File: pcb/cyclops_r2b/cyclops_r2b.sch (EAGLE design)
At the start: 54 parts, among them IC1 LM324N, IC2 317, IC3 REF02

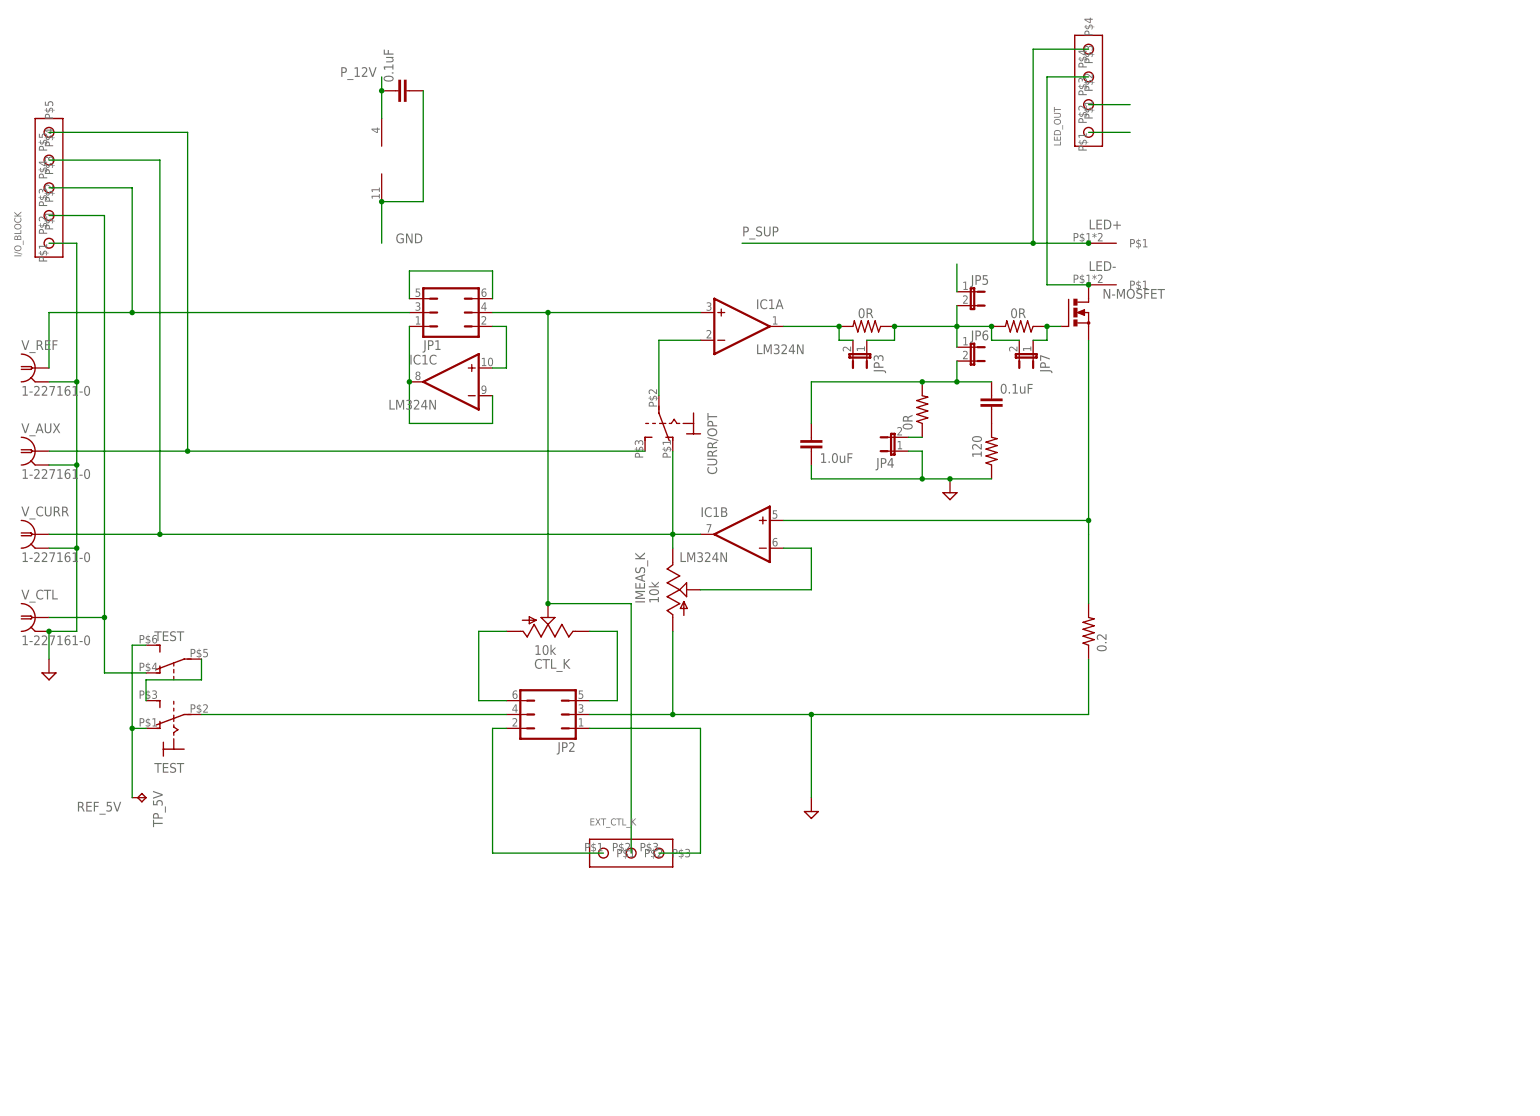
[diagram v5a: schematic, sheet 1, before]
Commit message: Revision 2b of the cyclops driver, ready for OSH Park.
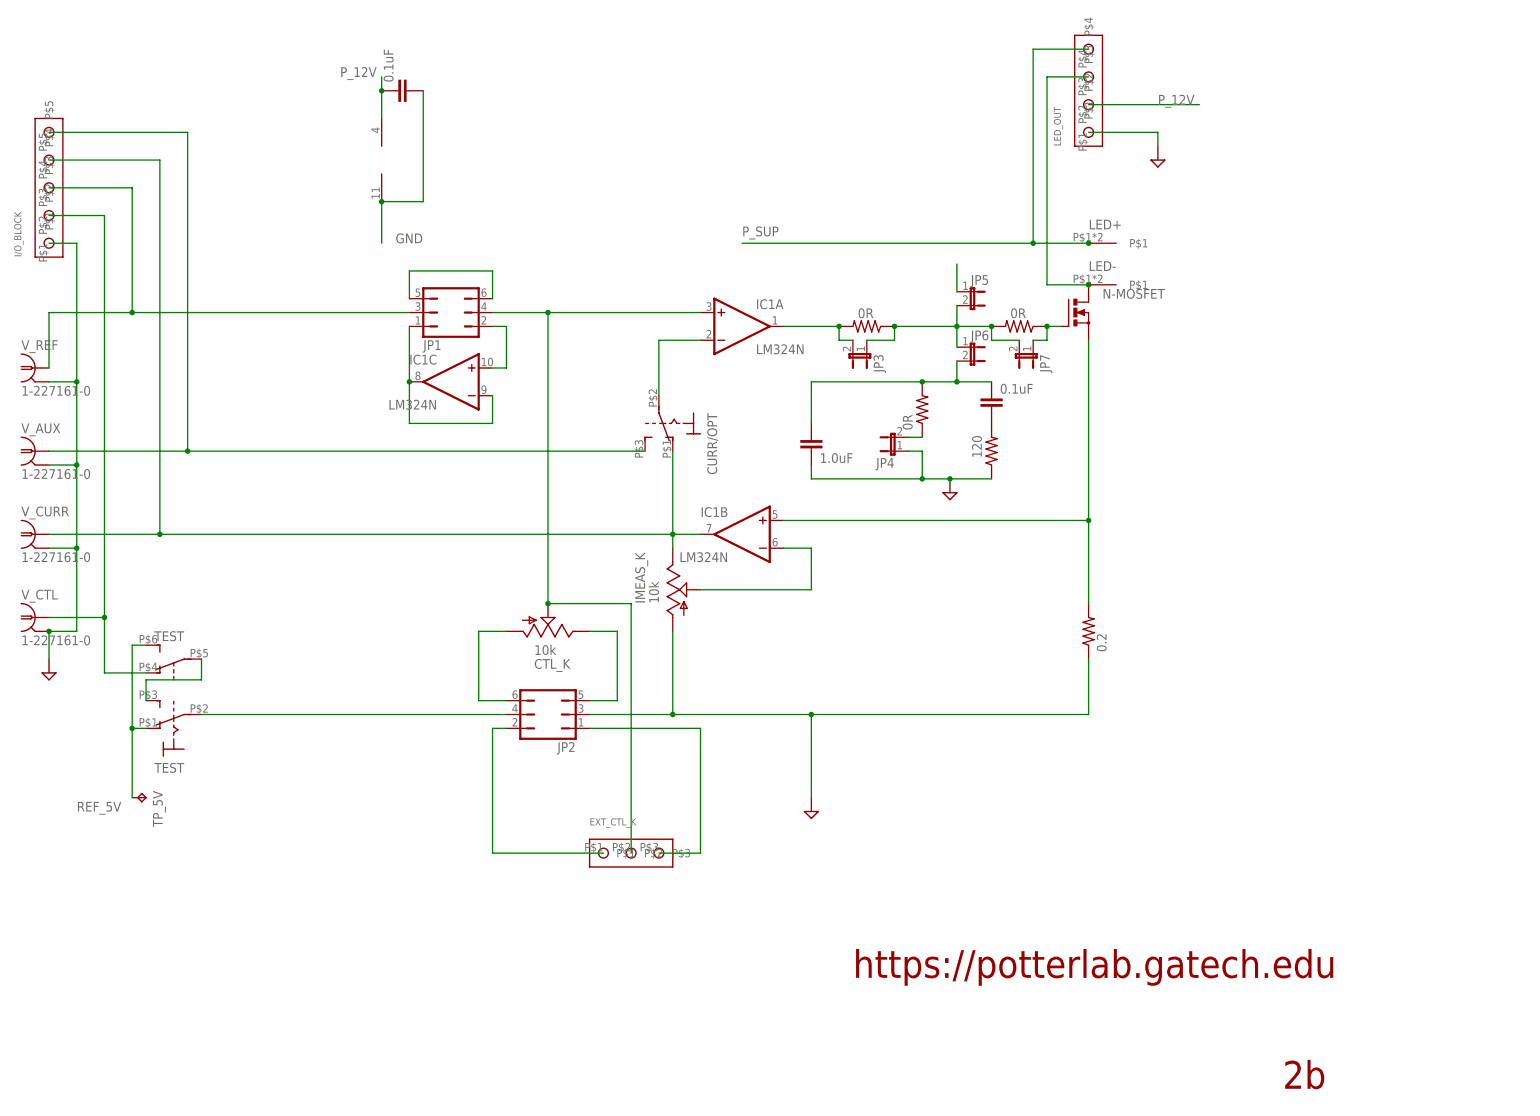
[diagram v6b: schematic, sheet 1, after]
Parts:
- C7: value 10u -> 10uF
- CTL_K, IMEAS_K, REF_ADJ, REG_ADJ: device HOSS:TRIM_US-RJ6S -> cyclops:TRIM_US-RJ6S
- R_CURR: device HOSS:R-US_ -> cyclops:R-US_0617/22
- U$1: device HOSS:NXT-FUSE -> cyclops:NXT-FUSE
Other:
- note added: "2b"
- note added: "https://potterlab.gatech.edu"
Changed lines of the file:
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@@
 </classes>
 <parts>
-<part name="R_CURR" library="HOSS" deviceset="R-US_" device="" value="0.2"/>
+<part name="R_CURR" library="cyclops" deviceset="R-US_" device="0617/22" value="0.2"/>
 <part name="SUPPLY2" library="supply2" deviceset="GND" device=""/>
 <part name="SUPPLY4" library="supply2" deviceset="GND" device=""/>
@@
 <part name="TEST" library="HOSS" deviceset="SP3T_SWITCH" device=""/>
 <part name="CURR/OPT" library="HOSS" deviceset="SPST_SWITCH" device=""/>
-<part name="IMEAS_K" library="HOSS" deviceset="TRIM_US-" device="RJ6S" value="10k"/>
-<part name="CTL_K" library="HOSS" deviceset="TRIM_US-" device="RJ6S" value="10k"/>
+<part name="IMEAS_K" library="cyclops" deviceset="TRIM_US-" device="RJ6S" value="10k"/>
+<part name="CTL_K" library="cyclops" deviceset="TRIM_US-" device="RJ6S" value="10k"/>
 <part name="LED+" library="cyclops" deviceset="BANANA_TO_BOARD" device=""/>
 <part name="LED-" library="cyclops" deviceset="BANANA_TO_BOARD" device=""/>
@@
 <part name="N-MOSFET" library="transistor-power" deviceset="PMOSFET_N" device="TO220BH"/>
 <part name="JP6" library="jumper" deviceset="JP1E" device=""/>
-<part name="TP_5V" library="testpad" deviceset="TP" device="PAD1-13"/>
+<part name="TP_5V" library="testpad" deviceset="TP" device="PAD1-13" value=""/>
 <part name="JP5" library="jumper" deviceset="JP1E" device=""/>
 <part name="IC3" library="linear" deviceset="REF02" device="DIL08-LONG" value="REF02"/>
-<part name="REG_ADJ" library="HOSS" deviceset="TRIM_US-" device="RJ6S" value="5k"/>
-<part name="REF_ADJ" library="HOSS" deviceset="TRIM_US-" device="RJ6S" value="10k"/>
+<part name="REG_ADJ" library="cyclops" deviceset="TRIM_US-" device="RJ6S" value="5k"/>
+<part name="REF_ADJ" library="cyclops" deviceset="TRIM_US-" device="RJ6S" value="10k"/>
 <part name="SUPPLY5" library="supply2" deviceset="GND" device=""/>
 <part name="C4" library="rcl" deviceset="C-EU" device="050-024X044" value="0.1uF"/>
@@
 <part name="GND2" library="cyclops" deviceset="BANANA_TO_BOARD" device=""/>
 <part name="POW1" library="HOSS" deviceset="SCREW2" device=""/>
-<part name="C7" library="rcl" deviceset="C-EU" device="025-024X044" value="10u"/>
-<part name="U$1" library="HOSS" deviceset="NXT-FUSE" device="" value="FUSE &gt;2A"/>
+<part name="C7" library="rcl" deviceset="C-EU" device="025-024X044" value="10uF"/>
+<part name="U$1" library="cyclops" deviceset="NXT-FUSE" device="" value="FUSE &gt;2A"/>
 <part name="R4" library="HOSS" deviceset="R-US_" device="0207/7" value="0R"/>
 <part name="JP7" library="jumper" deviceset="JP1E" device=""/>
+<part name="FRAME1" library="frames" deviceset="FRAME_A_L" device=""/>
+<part name="FRAME2" library="frames" deviceset="FRAME_A_L" device=""/>
+<part name="FRAME3" library="frames" deviceset="FRAME_A_L" device=""/>
+<part name="SUPPLY1" library="supply2" deviceset="GND" device=""/>
 </parts>
 <sheets>
 <sheet>
 <plain>
+<text x="76.2" y="-35.56" size="5.08" layer="94">https://potterlab.gatech.edu</text>
+<text x="154.94" y="-55.88" size="5.08" layer="94">2b</text>
 </plain>
 <instances>
@@
 </instance>
 <instance part="JP7" gate="A" x="109.22" y="78.74" rot="R180"/>
+<instance part="FRAME1" gate="G$1" x="-106.68" y="-60.96"/>
+<instance part="FRAME1" gate="G$2" x="66.04" y="-60.96"/>
+<instance part="SUPPLY1" gate="GND" x="132.08" y="114.3" smashed="yes"/>
 </instances>
 <busses>
@@
 </segment>
 <segment>
-<wire x1="119.38" y1="124.46" x2="127" y2="124.46" width="0.1524" layer="91"/>
+<wire x1="119.38" y1="124.46" x2="139.7" y2="124.46" width="0.1524" layer="91"/>
 <pinref part="LED_OUT" gate="G$1" pin="P$2"/>
+<label x="132.08" y="124.46" size="1.778" layer="95"/>
 </segment>
 </net>
@@
 <net name="GND" class="0">
 <segment>
-<wire x1="119.38" y1="119.38" x2="127" y2="119.38" width="0.1524" layer="91"/>
+<wire x1="119.38" y1="119.38" x2="132.08" y2="119.38" width="0.1524" layer="91"/>
 <pinref part="LED_OUT" gate="G$1" pin="P$1"/>
+<pinref part="SUPPLY1" gate="GND" pin="GND"/>
+<wire x1="132.08" y1="119.38" x2="132.08" y2="116.84" width="0.1524" layer="91"/>
 </segment>
 <segment>
@@
 <sheet>
 <plain>
+<text x="78.74" y="-38.1" size="5.08" layer="94">https://potterlab.gatech.edu</text>
+<text x="157.48" y="-58.42" size="5.08" layer="94">2b</text>
 </plain>
 <instances>
@@
 </instance>
 <instance part="ON" gate="G$1" x="20.32" y="55.88"/>
+<instance part="FRAME2" gate="G$1" x="-104.14" y="-63.5"/>
+<instance part="FRAME2" gate="G$2" x="68.58" y="-63.5"/>
 </instances>
 <busses>
@@
 <sheet>
 <plain>
+<text x="55.88" y="-53.34" size="5.08" layer="94">https://potterlab.gatech.edu</text>
+<text x="134.62" y="-73.66" size="5.08" layer="94">2b</text>
 </plain>
 <instances>
@@
 <instance part="C7" gate="G$1" x="33.02" y="63.5"/>
 <instance part="U$1" gate="G$1" x="22.86" y="50.8"/>
+<instance part="FRAME3" gate="G$1" x="-127" y="-78.74"/>
+<instance part="FRAME3" gate="G$2" x="45.72" y="-78.74"/>
 </instances>
 <busses>
@@
 <pinref part="U$1" gate="G$1" pin="P$4"/>
 <pinref part="U$1" gate="G$1" pin="P$3"/>
-</segment>
-</net>
+<label x="38.1" y="53.34" size="1.778" layer="95"/>
+</segment>
+</net>
